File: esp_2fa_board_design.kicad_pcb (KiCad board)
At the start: 2 copper layers, 82 x 45 mm, 53 parts, among them IC1 TPS22919DCKR, J1 Conn_01x06_Female, J2 TYPE-C-31-M-17, J3 Conn_01x02_Female, Q1 DMP2305U-7, SW5 POWER SWITCH, U1 ESP32-WROOM-32, U2 DS3231M, U3 MCP73831-2-OT, U4 TPS63001

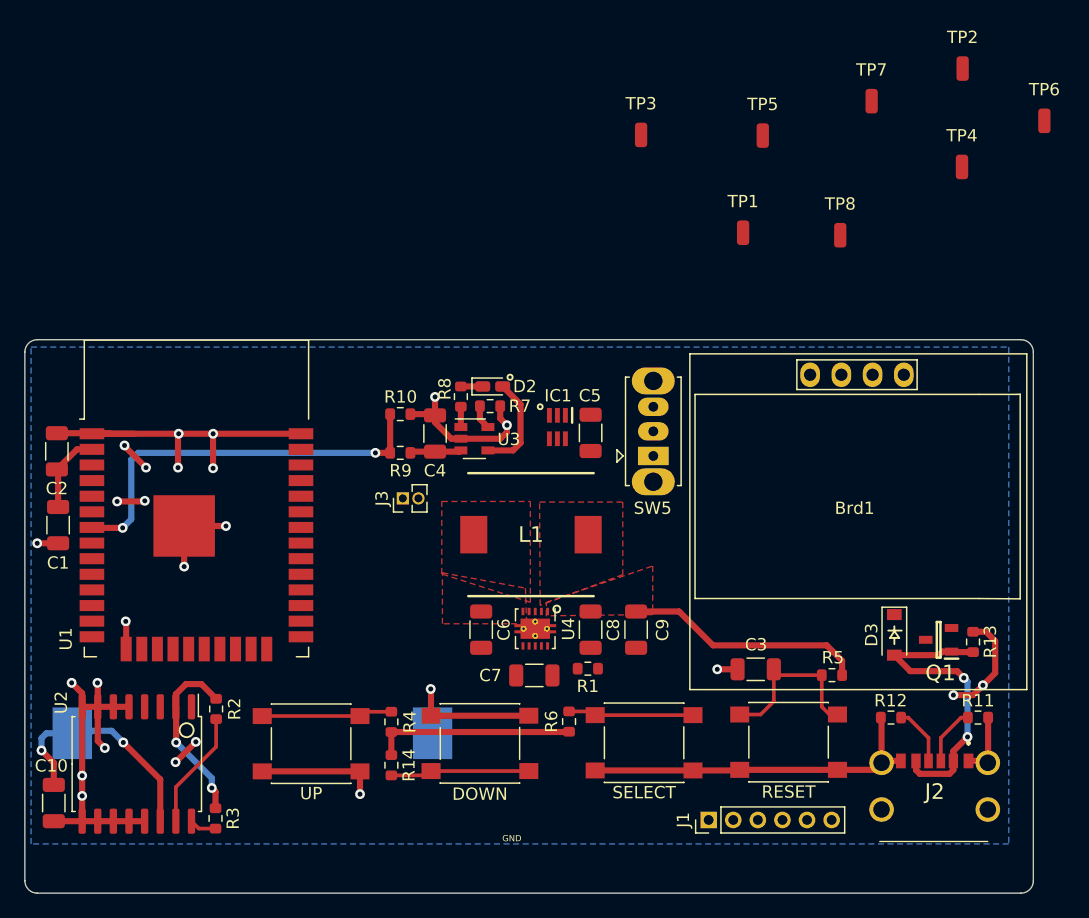
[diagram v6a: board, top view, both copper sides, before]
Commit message: Partially completed routing, regulator section remains
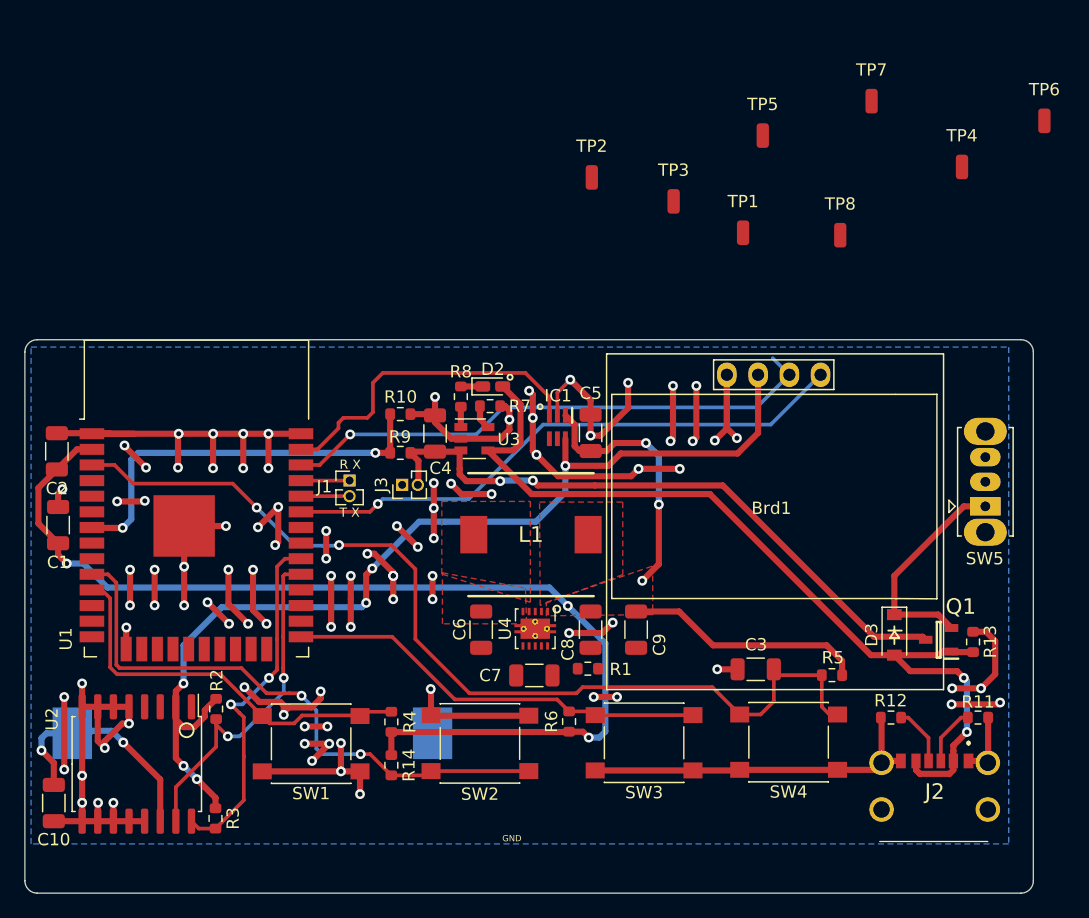
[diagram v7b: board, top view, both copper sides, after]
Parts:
- J1: value Conn_01x06_Female -> Conn_01x02_Female; footprint Connector_PinHeader_2.00mm:PinHeader_1x06_P2.00mm_Vertical -> Connector_PinHeader_1.27mm:PinHeader_1x02_P1.27mm_Vertical
- moved J1 40.2 mm to (116.4, 91.5), turned to 0 degrees
- moved TP2 31.4 mm to (136.1, 66.8)
- moved SW5 27.3 mm to (168.1, 93.5)
- moved Brd1 6.77 mm to (150.7, 93.5)
- moved TP3 6.02 mm to (142.8, 68.8)
- moved J3 1.10 mm to (120.7, 91.8)
- turned C1 to 90 degrees
- turned C5 to 270 degrees
- renumbered UP to SW1, DOWN to SW2, SELECT to SW3, RESET to SW4
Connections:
- J1 pad 1: Net-(J1-Pad1) -> /TX
- J1 pad 2: /TX -> /RX
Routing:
- net GND: track 156.2 -> 304.9 mm, vias 26 -> 95
- net +3V3: track 42.5 -> 127.0 mm, vias 0 -> 6
- net /LOAD_SWITCH_VCC: track 14.7 -> 84.2 mm, vias 2 -> 6
- net /EN: track 14.0 -> 78.9 mm, vias 0 -> 2
- net +BATT: track 4.18 -> 52.4 mm, vias 0 -> 2
- net /IO21_SDA: track 0.00 -> 46.9 mm, vias 0 -> 1
- net /IO22_SCL: track 0.00 -> 44.7 mm, vias 0 -> 1
- net VBUS: track 33.2 -> 73.1 mm
- net /IO25: track 11.3 -> 48.2 mm, vias 0 -> 2
- net /IO18_SCL: track 2.20 -> 29.2 mm, vias 0 -> 2
- net /IO23: track 0.00 -> 26.8 mm
- net /BOOT: track 10.2 -> 34.5 mm
- net /IO26: track 10.6 -> 32.6 mm
- net /IO5_SDA: track 9.66 -> 28.4 mm, vias 0 -> 2
- net /V_INPUT: track 0.00 -> 18.0 mm
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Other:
- board text added: "R X"
- board text added: "T X"

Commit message: Updated pcb design to reduce routes in the ground plane
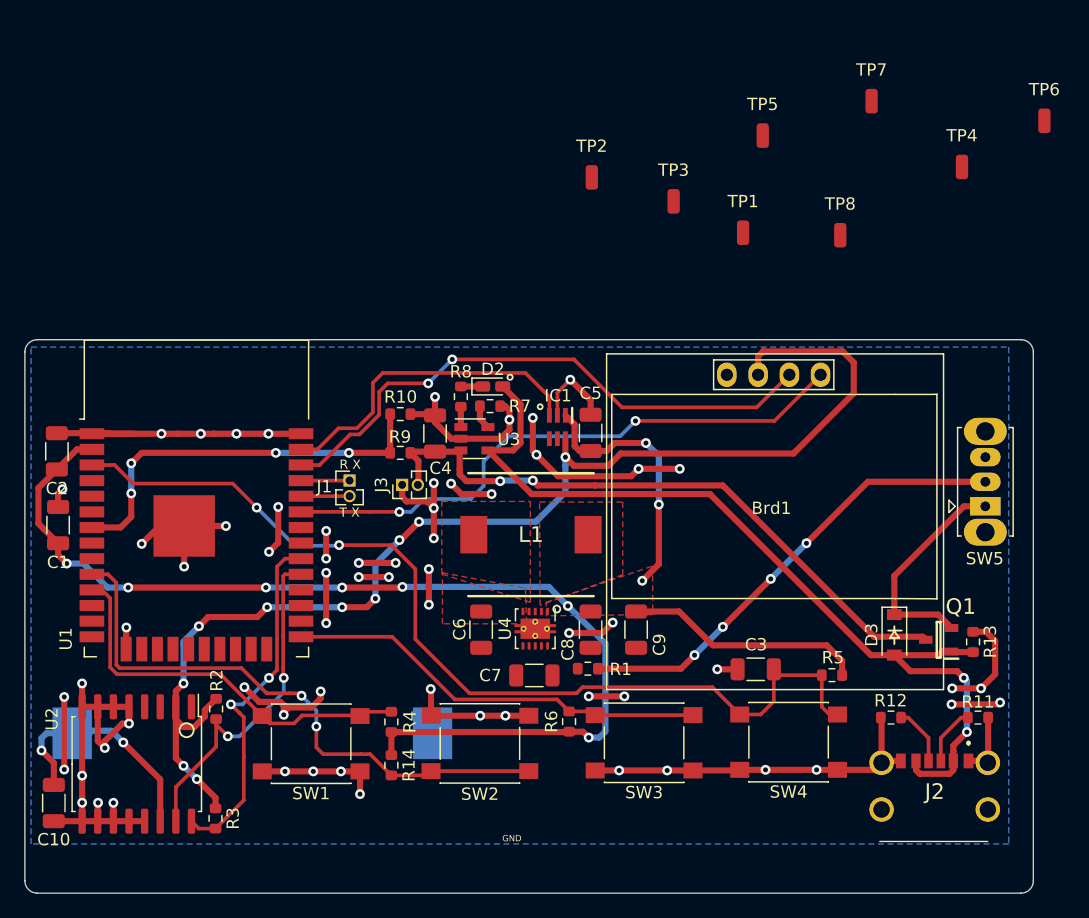
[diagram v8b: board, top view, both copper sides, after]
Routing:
- net GND: track 304.9 -> 231.4 mm, vias 95 -> 66
- net Net-(C6-Pad1): track 0.00 -> 37.8 mm, vias 0 -> 4
- net /LOAD_SWITCH_VCC: track 84.2 -> 101.6 mm, vias 6 -> 10
- net /IO22_SCL: track 44.7 -> 47.1 mm, vias 1 -> 2
- net /IO21_SDA: track 46.9 -> 48.0 mm, vias 1 -> 2
- net /A1_7_BATT: track 32.8 -> 32.5 mm, vias 2 -> 4
- net +3V3: track 127.0 -> 127.1 mm, vias 6 -> 10
